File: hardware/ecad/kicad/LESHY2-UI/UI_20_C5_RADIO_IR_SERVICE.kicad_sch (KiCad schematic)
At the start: 0 parts

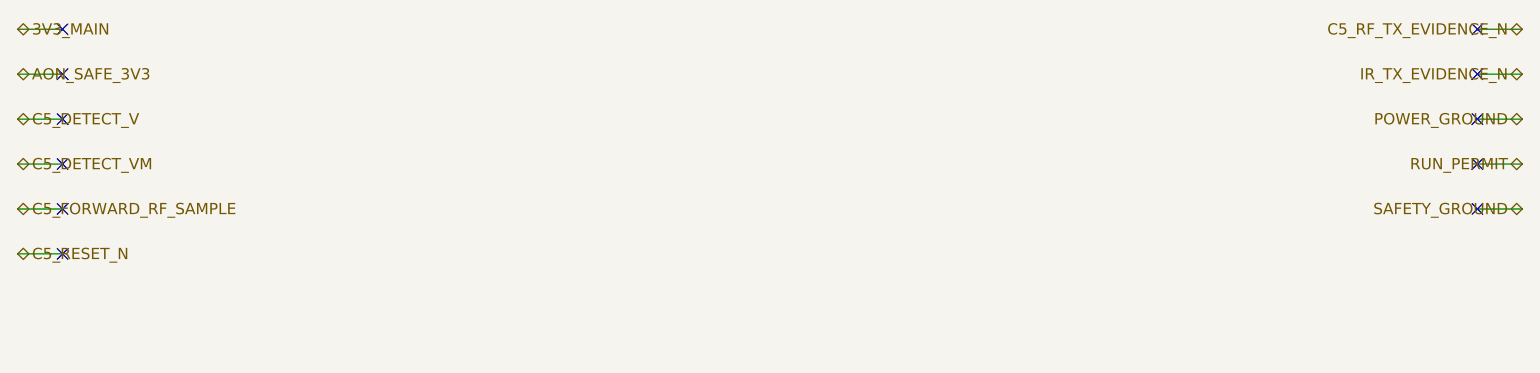
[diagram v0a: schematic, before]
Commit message: Complete H2.2.2 S3 core schematic
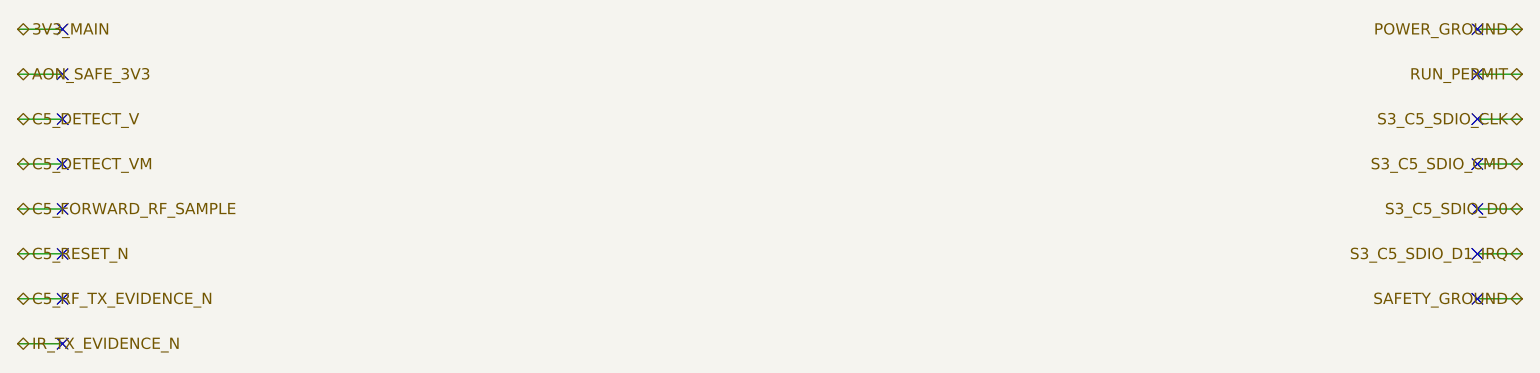
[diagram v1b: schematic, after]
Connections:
- no-connect marks 11 -> 15
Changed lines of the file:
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@@
 	(hierarchical_label "C5_RF_TX_EVIDENCE_N"
+		(shape bidirectional)
+		(at 20.32 50.80 0)
+		(effects (font (size 1.27 1.27)))
+	)
+	(wire
+		(pts (xy 20.32 50.80) (xy 25.40 50.80))
+		(stroke (width 0) (type default))
+	)
+	(no_connect (at 25.40 50.80)
+	)
+	(hierarchical_label "IR_TX_EVIDENCE_N"
+		(shape bidirectional)
+		(at 20.32 55.88 0)
+		(effects (font (size 1.27 1.27)))
+	)
+	(wire
+		(pts (xy 20.32 55.88) (xy 25.40 55.88))
+		(stroke (width 0) (type default))
+	)
+	(no_connect (at 25.40 55.88)
+	)
+	(hierarchical_label "POWER_GROUND"
 		(shape bidirectional)
 		(at 190.50 20.32 180)
@@
 	(no_connect (at 185.42 20.32)
 	)
-	(hierarchical_label "IR_TX_EVIDENCE_N"
+	(hierarchical_label "RUN_PERMIT"
 		(shape bidirectional)
 		(at 190.50 25.40 180)
@@
 	(no_connect (at 185.42 25.40)
 	)
-	(hierarchical_label "POWER_GROUND"
+	(hierarchical_label "S3_C5_SDIO_CLK"
 		(shape bidirectional)
 		(at 190.50 30.48 180)
@@
 	(no_connect (at 185.42 30.48)
 	)
-	(hierarchical_label "RUN_PERMIT"
+	(hierarchical_label "S3_C5_SDIO_CMD"
 		(shape bidirectional)
 		(at 190.50 35.56 180)
@@
 	(no_connect (at 185.42 35.56)
 	)
-	(hierarchical_label "SAFETY_GROUND"
+	(hierarchical_label "S3_C5_SDIO_D0"
 		(shape bidirectional)
 		(at 190.50 40.64 180)
@@
 	(no_connect (at 185.42 40.64)
 	)
+	(hierarchical_label "S3_C5_SDIO_D1_IRQ"
+		(shape bidirectional)
+		(at 190.50 45.72 180)
+		(effects (font (size 1.27 1.27)) (justify right))
+	)
+	(wire
+		(pts (xy 190.50 45.72) (xy 185.42 45.72))
+		(stroke (width 0) (type default))
+	)
+	(no_connect (at 185.42 45.72)
+	)
+	(hierarchical_label "SAFETY_GROUND"
+		(shape bidirectional)
+		(at 190.50 50.80 180)
+		(effects (font (size 1.27 1.27)) (justify right))
+	)
+	(wire
+		(pts (xy 190.50 50.80) (xy 185.42 50.80))
+		(stroke (width 0) (type default))
+	)
+	(no_connect (at 185.42 50.80)
+	)
 	(sheet_instances

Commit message: complete exact H2.2.6 C5 radio and IR schematic
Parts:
- added C1: Murata GRM1555C1H390JA01D, Capacitor_SMD:C_0402_1005Metric, symbol Leshy2:UI20_C5_DETECTOR_INPUT_CAP
- added C10: TDK C1005X7R1H104K050BB, Capacitor_SMD:C_0402_1005Metric, symbol Leshy2:UI20_C5_SERVICE_USB_SWITCH_BYPASS
- added C11: TDK C1005X7R1H104K050BB, Capacitor_SMD:C_0402_1005Metric, symbol Leshy2:UI20_IR_SAFE_GATE_BYPASS
- added C2: KEMET C0402C330J5GACTU, Capacitor_SMD:C_0402_1005Metric, symbol Leshy2:UI20_C5_DETECTOR_OUTPUT_CAP
- added C3: TDK C1005X7R1H104K050BB, Capacitor_SMD:C_0402_1005Metric, symbol Leshy2:UI20_C5_DETECTOR_BYPASS
- added C4: TDK C1608X7R1C105K080AC, Capacitor_SMD:C_0603_1608Metric, symbol Leshy2:UI20_IR_POWER_INPUT_CAP
- added C5: Murata GRM188R60J106ME47D, Capacitor_SMD:C_0603_1608Metric, symbol Leshy2:UI20_IR_POWER_OUTPUT_CAP
- added C6: TDK C1005X7R1H104K050BB, Capacitor_SMD:C_0402_1005Metric, symbol Leshy2:UI20_IR_POWER_OUTPUT_BYPASS
- added C7: Murata GRM188Z71A475ME15D, Capacitor_SMD:C_0603_1608Metric, symbol Leshy2:UI20_IR_DEMOD_SUPPLY_CAP
- added C8: Murata GRM188Z71A475ME15D, Capacitor_SMD:C_0603_1608Metric, symbol Leshy2:UI20_IR_CARRIER_SUPPLY_CAP
- added C9: TDK C1005X7R1H104K050BB, Capacitor_SMD:C_0402_1005Metric, symbol Leshy2:UI20_IR_RETURN_BUFFER_BYPASS
- added D1: Vishay VSMY14940, Leshy2:VSMY14940, symbol Leshy2:UI20_IR_EMITTER
- added D2: Texas Instruments TPD2EUSB30ADRTR, Package_TO_SOT_SMD:SOT-23, symbol Leshy2:UI20_C5_SERVICE_USB_ESD
- added D3: Texas Instruments TPD4E05U06DQAR, Package_SON:USON-10_2.5x1.0mm_P0.5mm, symbol Leshy2:UI20_C5_DBG_ESD
- added J1: GCT RFPC-SMA32-FN-175-A, Leshy2:RFPC-SMA32-FN-175-A, symbol Leshy2:UI20_C5_EXTERNAL_RP_SMA
- added J2: Hirose U.FL-R-SMT-1(10), Connector_Coaxial:U.FL_Hirose_U.FL-R-SMT-1_Vertical, symbol Leshy2:UI20_C5_RF_BOARD_CONNECTOR
- added J3: GCT USB4105-GF-A, Connector_USB:USB_C_Receptacle_GCT_USB4105-xx-A_16P_TopMnt_Horizontal, symbol Leshy2:UI20_C5_SERVICE_USB_CONNECTOR
- added J4: Samtec FTSH-105-01-L-DV-K-P-TR, Leshy2:FTSH-105-01-L-DV-K-P-TR, symbol Leshy2:UI20_C5_DBG_HEADER
- added Q1: Diodes Incorporated DMN2056U-7, Package_TO_SOT_SMD:SOT-23, symbol Leshy2:UI20_IR_TX_MOSFET
- added R1: Yageo RC0402FR-0749R9L, Resistor_SMD:R_0402_1005Metric, symbol Leshy2:UI20_C5_RF_COUPLER_TERMINATION
- added R10: Yageo RC0402FR-0710KL, Resistor_SMD:R_0402_1005Metric, symbol Leshy2:UI20_IR_DEMOD_HOST_PULLUP
- added R11: Yageo RC0402FR-0710KL, Resistor_SMD:R_0402_1005Metric, symbol Leshy2:UI20_IR_CARRIER_HOST_PULLUP
- added R12: Yageo RC1206FR-0733RL, Resistor_SMD:R_1206_3216Metric, symbol Leshy2:UI20_IR_EMITTER_LIMIT
- added R13: Yageo RC0402FR-07100RL, Resistor_SMD:R_0402_1005Metric, symbol Leshy2:UI20_IR_TX_GATE_SERIES
- added R14: Yageo RC0402FR-0710KL, Resistor_SMD:R_0402_1005Metric, symbol Leshy2:UI20_IR_TX_GATE_PULLDOWN
- added R15: Yageo RC0402FR-075K1L, Resistor_SMD:R_0402_1005Metric, symbol Leshy2:UI20_C5_SERVICE_USB_CC1_RD
- added R16: Yageo RC0402FR-075K1L, Resistor_SMD:R_0402_1005Metric, symbol Leshy2:UI20_C5_SERVICE_USB_CC2_RD
- added R17: Yageo RC0402FR-071ML, Resistor_SMD:R_0402_1005Metric, symbol Leshy2:UI20_C5_SERVICE_USB_VBUS_BLEEDER
- added R18: Panasonic ERJ-2RKF22R0X, Resistor_SMD:R_0402_1005Metric, symbol Leshy2:UI20_C5_SERVICE_USB_DM_SERIES
- added R19: Panasonic ERJ-2RKF22R0X, Resistor_SMD:R_0402_1005Metric, symbol Leshy2:UI20_C5_SERVICE_USB_DP_SERIES
- added R2: Yageo RC0402FR-0710KL, Resistor_SMD:R_0402_1005Metric, symbol Leshy2:UI20_C5_DETECTOR_FEEDBACK_RES
- added R20: Yageo RC0402FR-071KL, Resistor_SMD:R_0402_1005Metric, symbol Leshy2:UI20_C5_DBG_VTREF_SERIES
- added R21: Yageo RC0402FR-071KL, Resistor_SMD:R_0402_1005Metric, symbol Leshy2:UI20_C5_DBG_RESET_SERIES
- added R22: Yageo RC0402FR-071KL, Resistor_SMD:R_0402_1005Metric, symbol Leshy2:UI20_C5_DBG_BOOT_SERIES
- added R23: Yageo RC0402FR-07470RL, Resistor_SMD:R_0402_1005Metric, symbol Leshy2:UI20_C5_DBG0_SERIES
- added R24: Yageo RC0402FR-07470RL, Resistor_SMD:R_0402_1005Metric, symbol Leshy2:UI20_C5_DBG1_SERIES
- added R25: Yageo RC0402FR-0710KL, Resistor_SMD:R_0402_1005Metric, symbol Leshy2:UI20_C5_DBG_ID0_STRAP
- added R26: Yageo RC0402FR-0710KL, Resistor_SMD:R_0402_1005Metric, symbol Leshy2:UI20_C5_DBG_ID1_STRAP
- added R27: Yageo RC0402FR-0710KL, Resistor_SMD:R_0402_1005Metric, symbol Leshy2:UI20_C5_BOOT_PULLUP
- added R28: Yageo RC0402FR-0710KL, Resistor_SMD:R_0402_1005Metric, symbol Leshy2:UI20_C5_GPIO27_PULLUP
- added R29: Yageo RC0402FR-0710KL, Resistor_SMD:R_0402_1005Metric, symbol Leshy2:UI20_C5_RESET_PULLUP
- added R3: Yageo RC0402FR-0710KL, Resistor_SMD:R_0402_1005Metric, symbol Leshy2:UI20_C5_DETECTOR_GROUND_RES
- added R4: Yageo RC0402FR-0710KL, Resistor_SMD:R_0402_1005Metric, symbol Leshy2:UI20_IR_POWER_ON_PULLDOWN
- added R5: Yageo RC0402FR-07100RL, Resistor_SMD:R_0402_1005Metric, symbol Leshy2:UI20_IR_DEMOD_SUPPLY_RES
- added R6: Yageo RC0402FR-07100RL, Resistor_SMD:R_0402_1005Metric, symbol Leshy2:UI20_IR_CARRIER_SUPPLY_RES
- added R7: Yageo RC0402FR-074K7L, Resistor_SMD:R_0402_1005Metric, symbol Leshy2:UI20_IR_CARRIER_PULLUP
- added R8: Yageo RC0402FR-07100RL, Resistor_SMD:R_0402_1005Metric, symbol Leshy2:UI20_IR_DEMOD_SERIES
- added R9: Yageo RC0402FR-07100RL, Resistor_SMD:R_0402_1005Metric, symbol Leshy2:UI20_IR_CARRIER_SERIES
- added SW1: Alps Alpine SKRTLAE010, Button_Switch_SMD:SW_Push_1P1T-MP_NO_Horizontal_Alps_SKRTLAE010, symbol Leshy2:UI20_C5_RESET_BUTTON
- added SW2: Alps Alpine SKRTLAE010, Button_Switch_SMD:SW_Push_1P1T-MP_NO_Horizontal_Alps_SKRTLAE010, symbol Leshy2:UI20_C5_BOOT_BUTTON
- added U1: ESP32-C5-WROOM-1U-N8R8, Leshy2:ESP32-C5-WROOM-1U, symbol Leshy2:UI20_C5
- added U2: KYOCERA AVX CP0603Q5425ENTR, Leshy2:CP0603Q5425ENTR, symbol Leshy2:UI20_C5_RF_COUPLER
- added U3: Texas Instruments TPS22919DCKR, Package_TO_SOT_SMD:SOT-363_SC-70-6, symbol Leshy2:UI20_IR_POWER_SWITCH
- added U4: Vishay TSOP95238TT, Leshy2:Vishay-Heimdall-SMD-TT, symbol Leshy2:UI20_IR_DEMOD
- added U5: Vishay TSMP95000TT, Leshy2:Vishay-Heimdall-SMD-TT, symbol Leshy2:UI20_IR_CARRIER
- added U6: Nexperia 74LVC2G126DC,125, Package_SO:VSSOP-8_2.3x2mm_P0.5mm, symbol Leshy2:UI20_IR_RETURN_BUFFER
- added U7: onsemi FSUSB42MUX, Package_SO:MSOP-10_3x3mm_P0.5mm, symbol Leshy2:UI20_C5_SERVICE_USB_SWITCH
- added U8: SN74LVC1G08DCKR, Package_TO_SOT_SMD:Texas_R-PDSO-G5_DCK-5, symbol Leshy2:UI20_IR_SAFE_GATE
- added W1: TE Connectivity 2118651-2, symbol Leshy2:UI20_C5_RF_JUMPER
- added X1: ESP32-C5-WROOM-1U-N8R8 factory ANT1 U.FL, symbol Leshy2:UI20_C5_FACTORY_ANT1
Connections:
- net 3V3_MAIN: now also C10.1 (END_1), C4.1 (END_1), R10.2 (END_2), R11.2 (END_2), R12.1 (END_1), R20.2 (END_2), R25.2 (END_2), R27.1 (END_1), R28.1 (END_1), R29.1 (END_1), U1.2 (3V3), U3.1 (IN), U7.1 (VCC)
- net AON_SAFE_3V3: now also C11.1 (END_1), C3.1 (END_1), U8.5 (VCC)
- net C5_DETECT_V: now also C2.1 (END_1), R2.1 (END_1)
- net C5_DETECT_VM: now also R2.2 (END_2), R3.1 (END_1)
- net C5_FORWARD_RF_SAMPLE: now also C1.2 (END_2)
- net C5_RESET_N: now also R21.2 (END_2), R29.2 (END_2), U1.3 (EN)
- net C5_RF_TX_EVIDENCE_N: now also U1.21 (GPIO23)
- net IR_TX_EVIDENCE_N: now also U1.23 (GPIO24)
- net POWER_GROUND: now also C10.2 (END_2), C4.2 (END_2), C5.2 (END_2), C6.2 (END_2), C7.2 (END_2), C8.2 (END_2), C9.2 (END_2), D2.3 (GND), D3.3 (GND_3), D3.8 (GND_8), J3.A12_GND, J3.A1_GND, J3.B12_GND, J3.B1_GND, J3.SH (SHIELD), J4.2 (P2), J4.7 (P7), J4.9 (P9), Q1.2 (S), R14.2 (END_2), R15.2 (END_2), R16.2 (END_2), R17.2 (END_2), R26.2 (END_2), R4.2 (END_2), SW1.2 (NO), SW2.2 (NO), U1.1 (GND), U1.28 (GND), U1.29 (EPAD_GND), U1.30 (GND), U1.32 (GND), U3.2 (GND), U4.1 (GND_1), U4.4 (GND_4), U5.1 (GND_1), U5.4 (GND_4), U6.4 (GND), U7.10 (OE), U7.2 (SEL), U7.5 (GND)
- net RUN_PERMIT: now also U8.2 (B)
- net S3_C5_SDIO_CLK: now also U1.11 (GPIO9)
- net S3_C5_SDIO_CMD: now also U1.12 (GPIO10)
- net S3_C5_SDIO_D0: now also U1.10 (GPIO8)
- net S3_C5_SDIO_D1_IRQ: now also U1.9 (GPIO7)
- net SAFETY_GROUND: now also C11.2 (END_2), C2.2 (END_2), C3.2 (END_2), R3.2 (END_2), U8.3 (GND)
- new net C5_BOOT_N: R22.2 (END_2), R27.2 (END_2), U1.15 (GPIO28)
- new net C5_COUPLER_TERMINATION: R1.1 (END_1), U2.TERM (TERMINATION_50R)
- new net C5_DBG0_CONNECTOR: D3.4 (D2_PLUS), J4.5 (P5), R23.1 (END_1)
- new net C5_DBG1_CONNECTOR: D3.5 (D2_MINUS), J4.6 (P6), R24.1 (END_1)
- new net C5_DBG_BOOT_CONNECTOR_N: D3.2 (D1_MINUS), J4.4 (P4), R22.1 (END_1), SW2.1 (C1), SW2.3 (C2)
- new net C5_DBG_ID0: J4.8 (P8), R25.1 (END_1)
- new net C5_DBG_ID1: J4.10 (P10), R26.1 (END_1)
- new net C5_DBG_RESET_CONNECTOR_N: D3.1 (D1_PLUS), J4.3 (P3), R21.1 (END_1), SW1.1 (C1), SW1.3 (C2)
- new net C5_DBG_VTREF_SENSE: J4.1 (P1), R20.1 (END_1)
- new net C5_EXTERNAL_RF_50R: J1.1 (RF), U2.OUT (RF_OUT)
- new net C5_FORWARD_RF_SAMPLE_RAW: C1.1 (END_1), U2.CPL (COUPLED_FWD)
- new net C5_GPIO27_FIXED_HIGH: R28.2 (END_2), U1.18 (GPIO27)
- new net C5_MODULE_RF_50R: J2.1 (CENTER), U2.IN (RF_IN), W1.A (END_A), W1.B (END_B), X1.1 (FACTORY_UFL_ANT1)
- new net C5_RF_GROUND: J2.2 (SHELL), R1.2 (END_2)
- new net C5_SERVICE_CC1: J3.A5_CC1, R15.1 (END_1)
- new net C5_SERVICE_CC2: J3.B5_CC2, R16.1 (END_1)
- new net C5_SERVICE_USB_DM_CONNECTOR: D2.2 (D_MINUS), J3.A7_DM, J3.B7_DM, U7.4 (D_MINUS)
- new net C5_SERVICE_USB_DM_SWITCHED: R18.1 (END_1), U7.6 (HSD1_MINUS)
- new net C5_SERVICE_USB_DP_CONNECTOR: D2.1 (D_PLUS), J3.A6_DP, J3.B6_DP, U7.3 (D_PLUS)
- new net C5_SERVICE_USB_DP_SWITCHED: R19.1 (END_1), U7.7 (HSD1_PLUS)
- new net C5_SERVICE_VBUS_SENSE_ONLY: J3.A4_VBUS, J3.A9_VBUS, J3.B4_VBUS, J3.B9_VBUS, R17.1 (END_1)
- new net C5_SMA_RF_GROUND: J1.2 (GROUND_TOP_LEFT), J1.3 (GROUND_TOP_RIGHT), J1.4 (GROUND_BOTTOM_LEFT), J1.5 (GROUND_BOTTOM_RIGHT)
- new net C5_UART_SERVICE_RX: R24.2 (END_2), U1.24 (GPIO12)
- new net C5_UART_SERVICE_TX: R23.2 (END_2), U1.25 (GPIO11)
- new net C5_USB_DM: R18.2 (END_2), U1.13 (GPIO13)
- new net C5_USB_DP: R19.2 (END_2), U1.14 (GPIO14)
- new net IR_CARRIER_BUFFERED_N: R9.1 (END_1), U6.3 (2Y)
- new net IR_CARRIER_LOCAL_N: R7.1 (END_1), U5.3 (CARRIER_OUT), U6.5 (2A)
- new net IR_CARRIER_VS: C8.1 (END_1), R6.2 (END_2), R7.2 (END_2), U5.2 (VS)
- new net IR_DEMOD_BUFFERED_N: R8.1 (END_1), U6.6 (1Y)
- new net IR_DEMOD_LOCAL_N: U4.3 (OUT), U6.2 (1A)
- new net IR_DEMOD_VS: C7.1 (END_1), R5.2 (END_2), U4.2 (VS)
- new net IR_FRONTEND_PWR_EN: R4.1 (END_1), U1.17 (GPIO4), U3.3 (ON)
- new net IR_LED_ANODE_LIMITED: D1.1 (ANODE), R12.2 (END_2)
- new net IR_LED_CATHODE: D1.2 (CATHODE), Q1.3 (D)
- new net IR_RX_CARRIER: R11.1 (END_1), R9.2 (END_2), U1.7 (GPIO1)
- new net IR_RX_DEMOD: R10.1 (END_1), R8.2 (END_2), U1.6 (GPIO0)
- new net IR_RX_QOD: C5.1 (END_1), C6.1 (END_1), C9.1 (END_1), R5.1 (END_1), R6.1 (END_1), U3.5 (QOD), U3.6 (VOUT), U6.1 (1OE), U6.7 (2OE), U6.8 (VCC)
- new net IR_TX_CARRIER: U1.8 (GPIO6), U8.1 (A)
- new net IR_TX_CARRIER_SAFE: R13.1 (END_1), U8.4 (Y)
- new net IR_TX_GATE: Q1.1 (G), R13.2 (END_2), R14.1 (END_1)
- no-connect marks 15 -> 18
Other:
- title: (none) -> Leshy2 — exact C5 native radio, IR and service

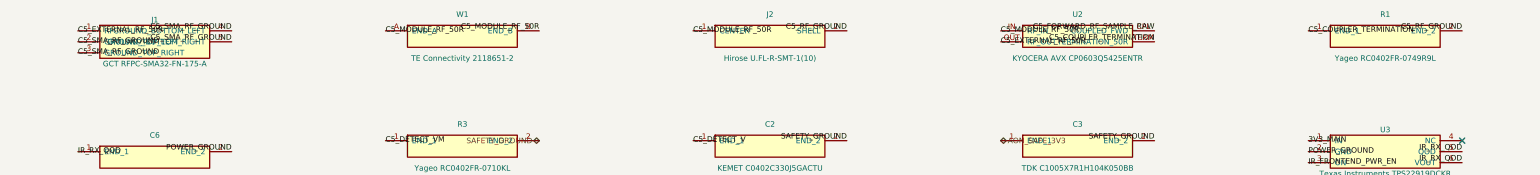
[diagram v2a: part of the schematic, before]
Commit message: complete exact H2.2.7 broadcast receiver schematic
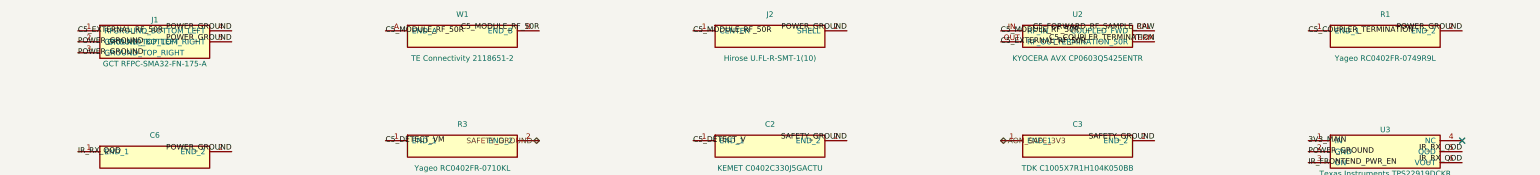
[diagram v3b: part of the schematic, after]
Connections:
- net C5_RF_GROUND is gone; now on net POWER_GROUND: J2.2 (SHELL), R1.2 (END_2)
- net C5_SMA_RF_GROUND is gone; now on net POWER_GROUND: J1.2 (GROUND_TOP_LEFT), J1.3 (GROUND_TOP_RIGHT), J1.4 (GROUND_BOTTOM_LEFT), J1.5 (GROUND_BOTTOM_RIGHT)
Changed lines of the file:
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@@
-		(effects (font (size 1.27 1.27)) (justify right bottom))
-	)
-	(label "C5_RF_GROUND"
-		(at 276.86 43.18 180)
-		(effects (font (size 1.27 1.27)) (justify right bottom))
-	)
-	(label "C5_RF_GROUND"
-		(at 419.10 43.18 180)
 		(effects (font (size 1.27 1.27)) (justify right bottom))
 	)
@@
 		(effects (font (size 1.27 1.27)))
 	)
-	(label "C5_SMA_RF_GROUND"
-		(at 99.06 45.72 0)
-		(effects (font (size 1.27 1.27)))
-	)
-	(label "C5_SMA_RF_GROUND"
-		(at 99.06 48.26 0)
-		(effects (font (size 1.27 1.27)))
-	)
-	(label "C5_SMA_RF_GROUND"
-		(at 134.62 43.18 180)
-		(effects (font (size 1.27 1.27)) (justify right bottom))
-	)
-	(label "C5_SMA_RF_GROUND"
-		(at 134.62 45.72 180)
-		(effects (font (size 1.27 1.27)) (justify right bottom))
-	)
 	(label "C5_UART_SERVICE_RX"
 		(at 63.50 60.96 180)
@@
 		(effects (font (size 1.27 1.27)) (justify right bottom))
 	)
+	(label "POWER_GROUND"
+		(at 99.06 45.72 0)
+		(effects (font (size 1.27 1.27)))
+	)
+	(label "POWER_GROUND"
+		(at 99.06 48.26 0)
+		(effects (font (size 1.27 1.27)))
+	)
+	(label "POWER_GROUND"
+		(at 134.62 43.18 180)
+		(effects (font (size 1.27 1.27)) (justify right bottom))
+	)
+	(label "POWER_GROUND"
+		(at 134.62 45.72 180)
+		(effects (font (size 1.27 1.27)) (justify right bottom))
+	)
+	(label "POWER_GROUND"
+		(at 276.86 43.18 180)
+		(effects (font (size 1.27 1.27)) (justify right bottom))
+	)
+	(label "POWER_GROUND"
+		(at 419.10 43.18 180)
+		(effects (font (size 1.27 1.27)) (justify right bottom))
+	)

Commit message: complete exact H2.2.10 UI test points
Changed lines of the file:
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@@
 		(effects (font (size 1.27 1.27)))
 	)
-	(label "C5_GPIO27_FIXED_HIGH"
+	(hierarchical_label "C5_GPIO27_FIXED_HIGH"
+		(shape bidirectional)
 		(at 63.50 45.72 180)
 		(effects (font (size 1.27 1.27)) (justify right bottom))
@@
 		(effects (font (size 1.27 1.27)))
 	)
-	(label "C5_SERVICE_VBUS_SENSE_ONLY"
+	(hierarchical_label "C5_SERVICE_VBUS_SENSE_ONLY"
+		(shape bidirectional)
 		(at 525.78 147.32 0)
 		(effects (font (size 1.27 1.27)))
@@
 		(effects (font (size 1.27 1.27)))
 	)
-	(label "IR_TX_CARRIER_SAFE"
+	(hierarchical_label "IR_TX_CARRIER_SAFE"
+		(shape bidirectional)
 		(at 312.42 144.78 0)
 		(effects (font (size 1.27 1.27)))

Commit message: complete H2 schematic review package
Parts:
- renumbered C1 to C20001, C2 to C20002, C3 to C20003, C4 to C20004, C5 to C20005, C6 to C20006, C7 to C20007, C8 to C20008, C9 to C20009, C10 to C20010, C11 to C20011, D1 to D20001, D2 to D20002, D3 to D20003, J1 to J20001, J2 to J20002, J3 to J20003, J4 to J20004, Q1 to Q20001, R1 to R20001, R2 to R20002, R3 to R20003, R4 to R20004, R5 to R20005, R6 to R20006, R7 to R20007, R8 to R20008, R9 to R20009, R10 to R20010, R11 to R20011, R12 to R20012, R13 to R20013, R14 to R20014, R15 to R20015, R16 to R20016, R17 to R20017, R18 to R20018, R19 to R20019, R20 to R20020, R21 to R20021, R22 to R20022, R23 to R20023, R24 to R20024, R25 to R20025, R26 to R20026, R27 to R20027, R28 to R20028, R29 to R20029, SW1 to SW20001, SW2 to SW20002, U1 to U20001, U2 to U20002, U3 to U20003, U4 to U20004, U5 to U20005, U6 to U20006, U7 to U20007, U8 to U20008, W1 to W20001, X1 to X20001

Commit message: Review H3.3.3 infrared electrical corners
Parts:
- added R20013: Yageo RC0402FR-0710KL, Resistor_SMD:R_0402_1005Metric, symbol Leshy2:UI20_IR_TX_CARRIER_PULLDOWN
- R20012: value Yageo RC1206FR-0733RL -> Yageo RC1206FR-0747RL
- renumbered R20013 to R20014, R20014 to R20015, R20015 to R20016, R20016 to R20017, R20017 to R20018, R20018 to R20019, R20019 to R20020, R20020 to R20021, R20021 to R20022, R20022 to R20023, R20023 to R20024, R20024 to R20025, R20025 to R20026, R20026 to R20027, R20027 to R20028, R20028 to R20029, R20029 to R20030
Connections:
- net IR_TX_CARRIER: now also R20013.1 (END_1)
- net SAFETY_GROUND: now also R20013.2 (END_2)
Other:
- moved on the sheet: C20010, C20011, D20002, D20003, J20003, J20004, R20014, R20015, R20016, R20017, R20018, R20019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

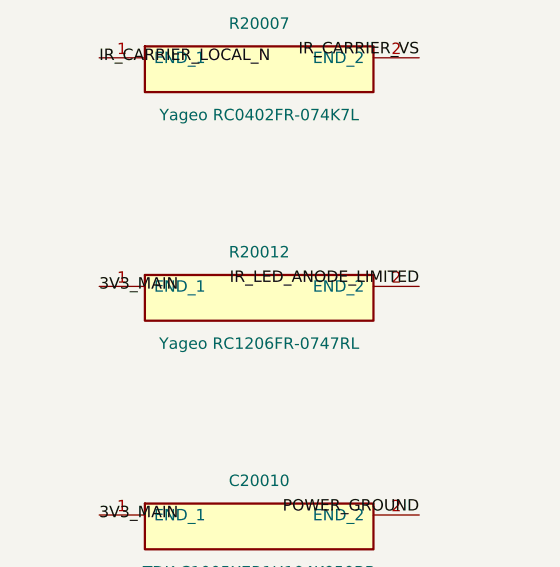
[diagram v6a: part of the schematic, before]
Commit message: review H3.6.2 single-fault containment
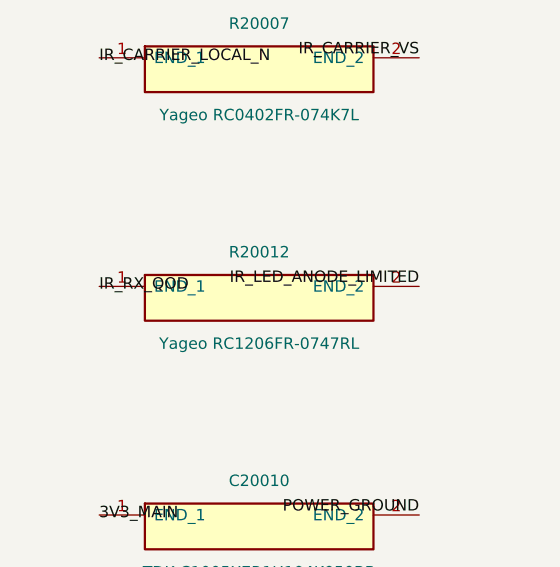
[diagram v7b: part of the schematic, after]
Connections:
- net 3V3_MAIN: no longer R20012.1 (END_1)
- net IR_RX_QOD: now also R20012.1 (END_1)
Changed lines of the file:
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@@
-	)
-	(label "3V3_MAIN"
-		(at 27.94 129.54 0)
-		(effects (font (size 1.27 1.27)))
 	)
 	(label "3V3_MAIN"
@@
 		(effects (font (size 1.27 1.27)))
 	)
+	(label "IR_RX_QOD"
+		(at 27.94 129.54 0)
+		(effects (font (size 1.27 1.27)))
+	)

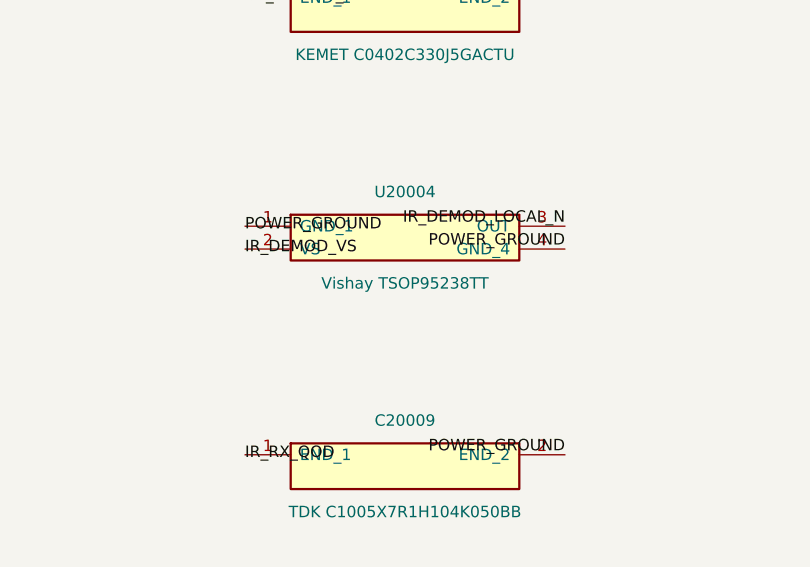
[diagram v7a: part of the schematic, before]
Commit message: hardware: replace full-reel IR receiver
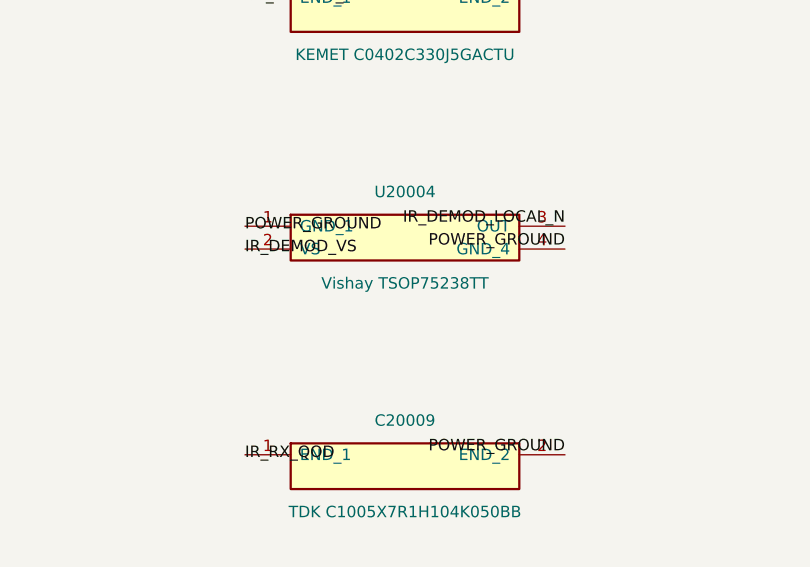
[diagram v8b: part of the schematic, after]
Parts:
- U20004: value Vishay TSOP95238TT -> Vishay TSOP75238TT
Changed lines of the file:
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@@
 			(effects (font (size 1.27 1.27)))
 		)
-		(property "Value" "Vishay TSOP95238TT"
+		(property "Value" "Vishay TSOP75238TT"
 			(at 259.08 100.33 0)
 			(show_name no)
